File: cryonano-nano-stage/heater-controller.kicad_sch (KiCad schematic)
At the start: 0 parts

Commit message: sch improved
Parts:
- added PS1: B2415S-1WR3, SamacSys_Parts:HLKB2405S2WR3, symbol symbols:BxxxxS-1WR3
- added PS3: B2415S-2WR3, symbol symbols:BxxxxS-2WR3
- added R27: 10k, Resistor_SMD:R_0603_1608Metric, symbol Device:R_Small
- added R37, R39: 1k2, Resistor_SMD:R_0603_1608Metric, symbol Device:R_Small
- added R40: 22R, Resistor_SMD:R_0603_1608Metric, symbol Device:R_Small
- added U3: 1ED3141MU12FXUMA1, SOIC127P600X175-8N, symbol symbols:1ED3141MU12FXUMA1
- added Z2: MM1W18, Diode_SMD:D_SOD-123, symbol symbols:MM1W18
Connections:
- new net: R39.1, U3.6 (OUTH)
- new net: R40.2, U3.2 (IN+)
- new net: R37.1, U3.7 (OUTL)
- new net +24V0IN: PS1.2 (+VIN), PS3.1 (+VIN)
- new net +3V3IN: U3.1 (VCC1)
- new net 0V0IN: U3.3 (IN-), U3.4 (GND1)
- new net M15V0: PS1.3 (-VO), PS3.4 (-VOUT), U3.5 (VCC2)
- new net M24V0IN: PS1.1 (GND), PS3.2 (GND)
- new net PWMIN: R40.1
- new net SW_G: R27.1, R37.2, R39.2, Z2.1 (C)
- new net SW_S: PS1.4 (+VO), PS3.6 (+VOUT), R27.2, U3.8 (VEE2), Z2.2 (A)
- no-connect marks 0 -> 1
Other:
- removed sheet High Side N-Mosfet Driver
- removed sheet High Side P-Mosfet Driver
- note removed: "Note: For load current higer than 5A, High-Side N-Mosfet is prefered."
- company: (none) -> Cryonano Labs Pvt. Ltd.
- title: (none) -> Nano stage controller

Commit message: sch improved
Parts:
- added C39: 10u, Capacitor_SMD:C_0805_2012Metric, symbol Device:C_Small
- added C40, C42: 100n, Capacitor_SMD:C_0603_1608Metric, symbol Device:C_Small
- added C41: 4.7u, Capacitor_SMD:C_0805_2012Metric, symbol Device:C_Small
- PS1: value B2415S-1WR3 -> BxxxxS-1WR3; footprint SamacSys_Parts:HLKB2405S2WR3 -> footprints:BxxxxS-1WR3
- PS3: value B2415S-2WR3 -> BxxxxS-2WR3; footprint (none) -> footprints:BxxxxS-2WR3
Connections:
- net +3V3IN: now also C41.1, C42.1
- net 0V0IN: now also C41.2, C42.2
- net M15V0: now also C39.2, C40.2
- net SW_S: now also C39.1, C40.1

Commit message: sch improved
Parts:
- added C58: 1u, Capacitor_SMD:C_0603_1608Metric, symbol Device:C_Small
- C39, C40: Voltage 16V -> 35V
- R37: value 1k2 -> 6R2
- R39: value 1k2 -> 10R
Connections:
- net +24V0IN: now also C58.1
- net M24V0IN: now also C58.2
- net SW_S: now also C39.2, C40.2, PS1.3 (-VO), PS3.4 (-VOUT); no longer C39.1, C40.1, PS1.4 (+VO), PS3.6 (+VOUT)
- removed net M15V0: C39.2, C40.2, PS1.3 (-VO), PS3.4 (-VOUT), U3.5 (VCC2)
- new net +15V0: C39.1, C40.1, PS1.4 (+VO), PS3.6 (+VOUT), U3.5 (VCC2)

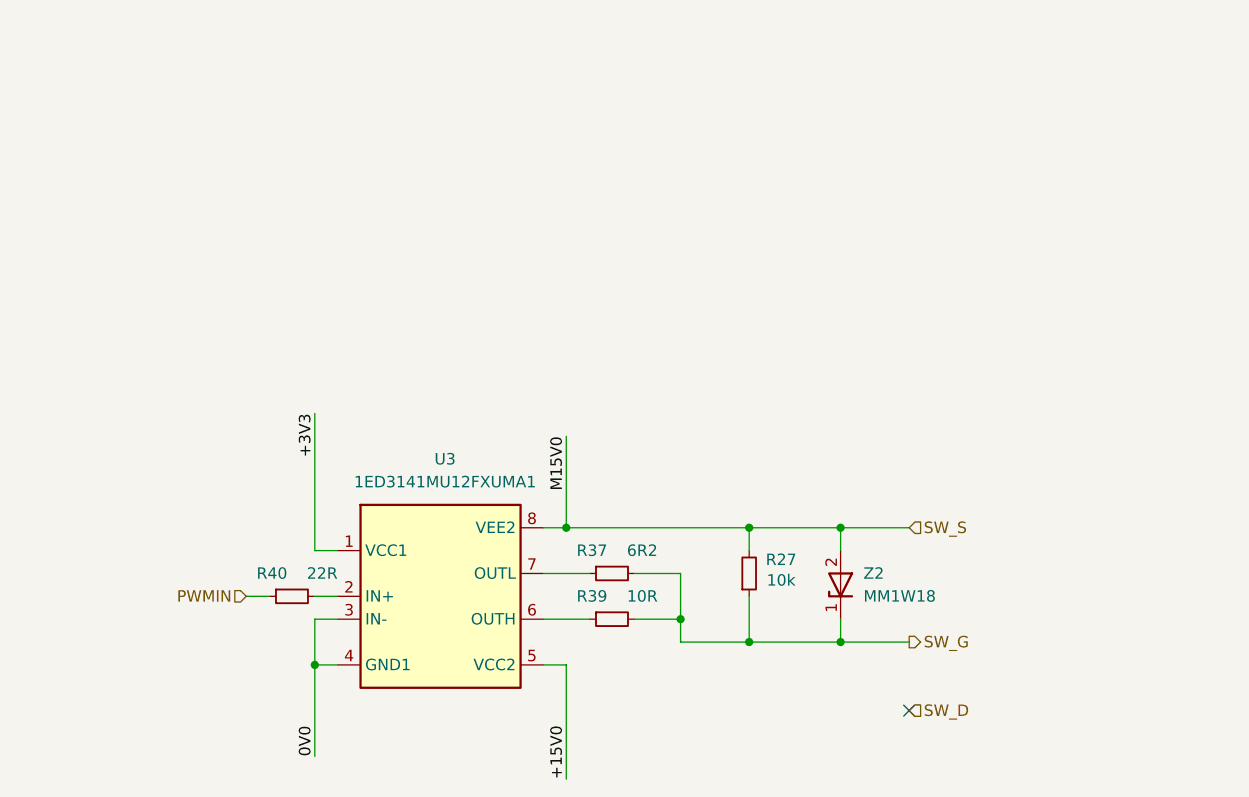
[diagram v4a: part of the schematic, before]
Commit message: pcb drc ok. 68 ohm matching pending
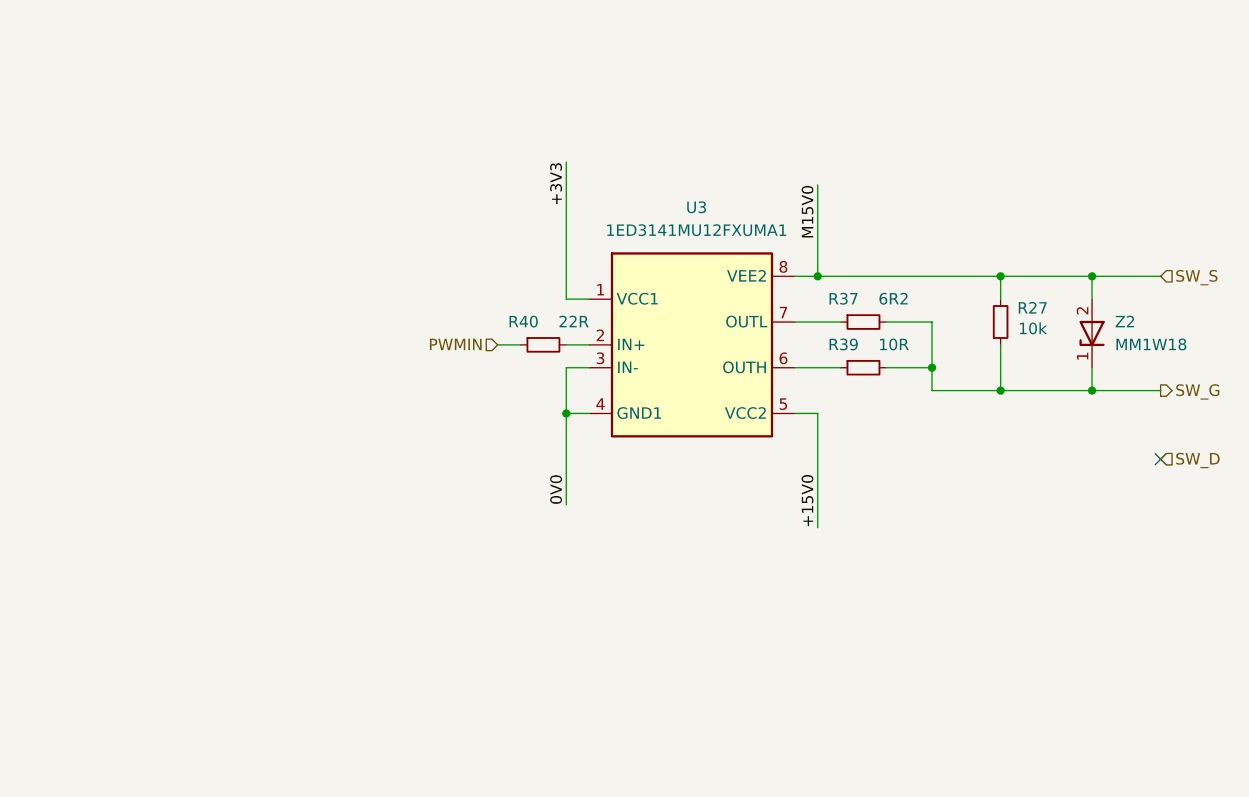
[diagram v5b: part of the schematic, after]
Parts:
- C39: footprint Capacitor_SMD:C_0805_2012Metric -> Capacitor_SMD:C_1210_3225Metric; Manufacturer (none) -> YAGEO; Order No. (none) -> CC1210KFX7R9BB106; Unit Price 10 (none) -> 31.1; Voltage 35V -> 50V
- C40: Manufacturer (none) -> KEMET; Order No. (none) -> C0603C104K5RAC7411; Unit Price 10 (none) -> 2.5; Voltage 35V -> 50V
- C41: Manufacturer (none) -> MURATA; Order No. (none) -> GRM21BR71C475KE51K; Unit Price 10 (none) -> 3
- C42: Manufacturer (none) -> KEMET; Order No. (none) -> C0603C104K5RAC7411; Tolerence 10% -> (none); Unit Price 10 (none) -> 2.5
- C58: footprint Capacitor_SMD:C_0603_1608Metric -> Capacitor_SMD:C_0805_2012Metric; Manufacturer (none) -> MURATA; Order No. (none) -> GCM21BR71H105KA03K; Unit Price 10 (none) -> 9.2
- U3: footprint SOIC127P600X175-8N -> footprints:SOIC127P600X175-8N; Manufacturer_Name Infineon -> (none); Manufacturer_Part_Number 1ED3141MU12FXUMA1 -> (none)
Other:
- moved on the sheet: R27, R37, R39, R40, U3, Z2

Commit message: bom adjusted
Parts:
- R27: Order No. (none) -> 0603/120mW
- R37: Order No. (none) -> ESR03EZPF6R20
- R39: Order No. (none) -> ESR03EZPJ100
- R40: value 22R -> 33R; Order No. (none) -> 0603/120mW
- Z2: Order No. (none) -> 18V, 1W, SOD-123 Zener
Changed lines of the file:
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@@
 			)
 		)
-		(property "Order No." ""
+		(property "Order No." "ESR03EZPJ100"
 			(at 134.62 99.06 0)
 			(hide yes)
@@
 			)
 		)
-		(property "Order No." ""
+		(property "Order No." "0603/120mW"
 			(at 149.86 93.98 90)
 			(hide yes)
@@
 			)
 		)
-		(property "Description" ""
+		(property "Description" "Zener Diode 18V 1W SOD-123"
 			(at 160.02 96.52 0)
 			(hide yes)
@@
 			)
 		)
+		(property "Order No." "18V, 1W, SOD-123 Zener "
+			(at 160.02 96.52 90)
+			(hide yes)
+			(show_name no)
+			(do_not_autoplace no)
+			(effects
+				(font
+					(size 1.27 1.27)
+				)
+			)
+		)
 		(pin "2"
 		)
@@
 			)
 		)
-		(property "Order No." ""
+		(property "Order No." "ESR03EZPF6R20"
 			(at 134.62 93.98 0)
 			(hide yes)
@@
 			)
 		)
-		(property "Value" "22R"
+		(property "Value" "33R"
 			(at 104.14 93.98 90)
 			(show_name no)
@@
 			)
 		)
-		(property "Order No." ""
+		(property "Order No." "0603/120mW"
 			(at 99.06 96.52 0)
 			(hide yes)

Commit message: drc ok, review schematic
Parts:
- removed U3: 1ED3141MU12FXUMA1, footprints:SOIC127P600X175-8N, symbol symbols:1ED3141MU12FXUMA1
- added C61: 100n, Capacitor_SMD:C_0603_1608Metric, symbol Device:C_Small
- added FB6: MH1608, Inductor_SMD:L_0603_1608Metric, symbol Device:FerriteBead
- added R28: 133k, Resistor_SMD:R_0603_1608Metric, symbol Device:R_Small
- added R97, R98: 33k, Resistor_SMD:R_0603_1608Metric, symbol Device:R_Small
- added U3: TLP2735(TP,E(O, footprints:SO-6L_10x3.84mm_P1.27mm, symbol symbols:TLP2735
- added U8: 1EDN7550BXTSA1, footprints:SOT95P280X145-6N, symbol symbols:1EDN7550BXTSA1
- C39: footprint Capacitor_SMD:C_1210_3225Metric -> Capacitor_SMD:C_0805_2012Metric; Manufacturer YAGEO -> (none); Order No. CC1210KFX7R9BB106 -> (none); Unit Price 10 31.1 -> (none)
- R40: value 33R -> 825R
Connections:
- net +15V0: now also FB6.1, U3.6 (VDD)
- net 0V0IN: now also U3.3 (C)
- net SW_G: now also R27.2; no longer R27.1
- net SW_S: now also R27.1, C61.2, R28.1, R98.1, U3.4 (GND), U8.2 (GND); no longer R27.2
- net at R39.1: now also U8.6 (OUT_SNK)
- net at R40.2: now also U3.1 (A)
- net at R37.1: now also U8.5 (OUT_SRC)
- new net: C61.1, FB6.2, U8.4 (VDD)
- new net: R98.2, U8.1 (IN-)
- new net: R28.2, R97.1, U3.5 (VO)
- new net: R97.2, U8.3 (IN+)
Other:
- moved on the sheet: R27, R37, R39, R40, Z2

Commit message: drc ok. chip level review pending
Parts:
- added C62: 100n, Capacitor_SMD:C_0603_1608Metric, symbol Device:C_Small
- added R96: 6R2, Resistor_SMD:R_0603_1608Metric, symbol Device:R_Small
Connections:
- net SW_G: now also C62.1
- net SW_S: now also R96.1
- new net: C62.2, R96.2
